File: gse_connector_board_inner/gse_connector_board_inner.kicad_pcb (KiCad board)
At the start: 2 copper layers, 52 x 27 mm, 27 parts, among them J1 arming_connector, J2 gse_com_connector, J3 chg_connector, J4 Conn_02x03_Top_Bottom, J5 Conn_02x02_Top_Bottom, U7 ISO1044BD, U9 MCP2562-E-SN

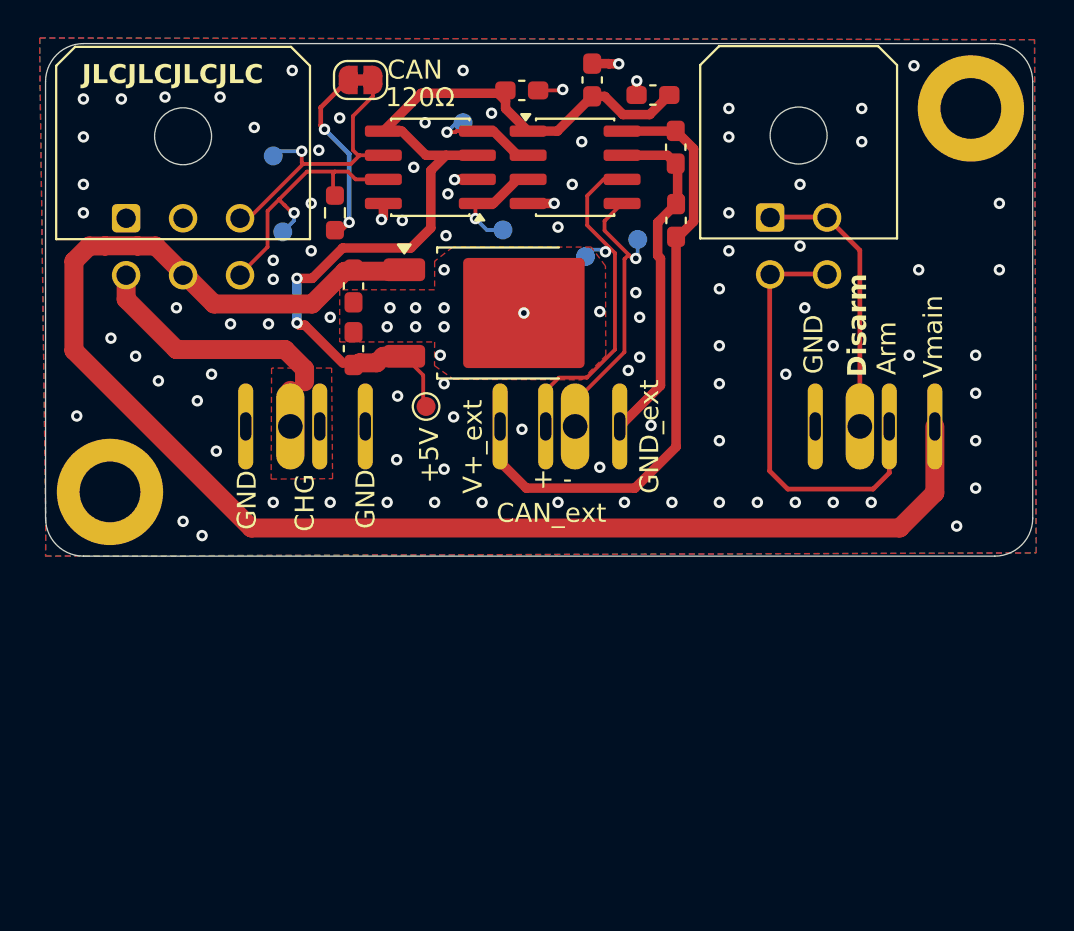
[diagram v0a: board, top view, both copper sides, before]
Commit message: first draft of rev3 with new pogo pins
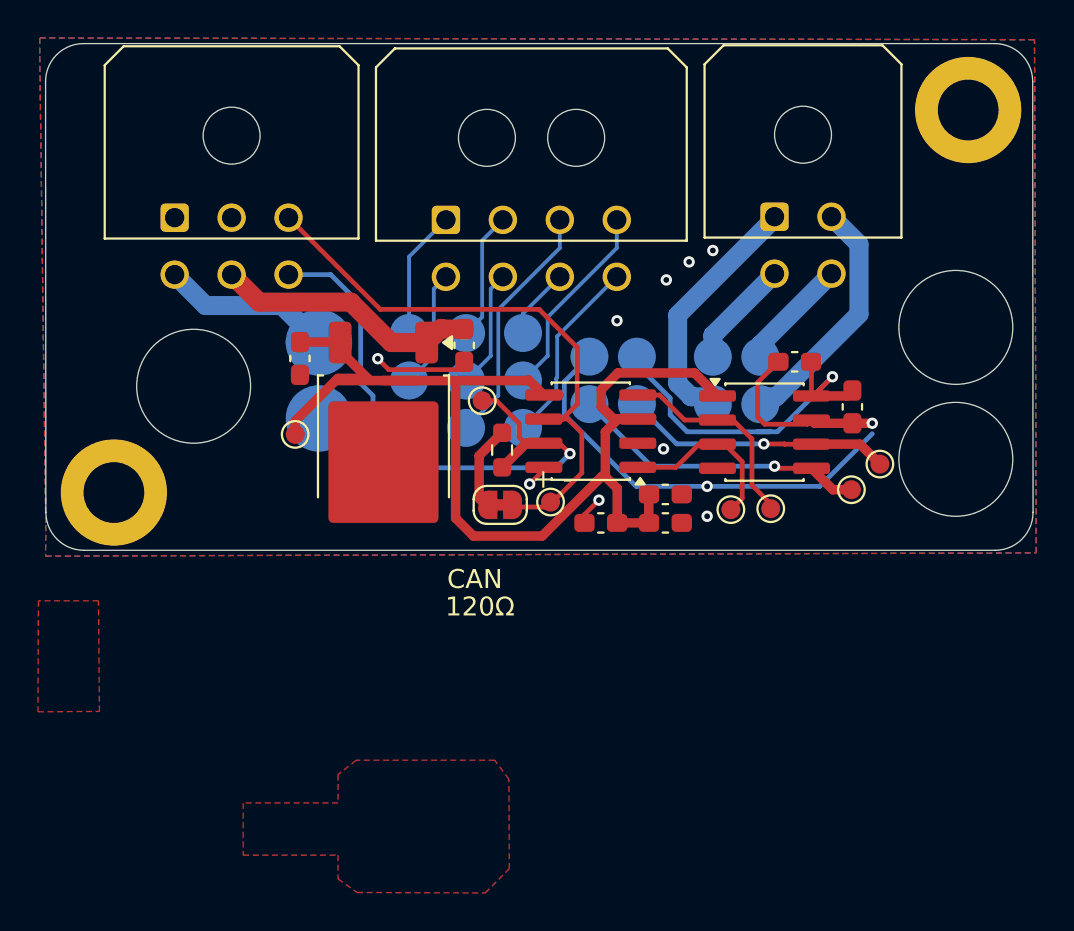
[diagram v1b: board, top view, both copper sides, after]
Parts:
- removed J1: arming_connector, custom_parts:4_pin_mag_con_new
- J2: value gse_com_connector -> Conn_01x19_Socket; footprint custom_parts:4_pin_mag_con_new -> custom_parts:tudsat_gse_connector_rev_1
- J3: value chg_connector -> ~; footprint custom_parts:4_pin_mag_con_new -> Connector_Molex:Molex_Micro-Fit_3.0_43045-0800_2x04_P3.00mm_Horizontal; moved to F.Cu
- TP1, TP2, TP3, TP4, TP5, TP6: moved to F.Cu
- moved H2 49.5 mm to (158.6, 56.5)
- moved H1 49.5 mm to (113.6, 76.7)
- moved TP5 26.0 mm to (148.2, 77.5), turned to 0 degrees
- moved JP4 23.6 mm to (133.9, 77.3)
- moved TP2 23.4 mm to (136.6, 77.2), turned to 0 degrees
- moved C29 23.3 mm to (139.2, 78.2), turned to 0 degrees
- moved C22 22.6 mm to (142.7, 76.8)
- moved C28 22.6 mm to (142.7, 78.2), turned to 180 degrees
- moved TP6 19.0 mm to (146.1, 77.5), turned to 0 degrees
- moved TP3 19.0 mm to (153.9, 75.2), turned to 0 degrees
- moved TP4 17.3 mm to (152.4, 76.5), turned to 0 degrees
- moved U7 17.2 mm to (147.9, 73.5)
- moved C24 16.5 mm to (152.5, 72.1)
- moved U9 16.3 mm to (138.7, 73.4)
- moved J3 16.1 mm to (131.1, 62.3), turned to 0 degrees
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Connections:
- J2 pad 1: +V_EXT -> arming_voltage
- J2 pad 2: CAN_ext+ -> arm
- J2 pad 3: CAN_ext- -> GND
- J2 pad 4: GND_EXT -> disarm
- J3 pad 1: GND -> TX+
- J3 pad 2: CHG -> RX+
- J3 pad 3: CHG -> NC1
- J3 pad 4: GND -> NC3
- J5 pad 1: disarm -> GND
- J5 pad 2: disarm -> arming_voltage
- J5 pad 3: arm -> disarm
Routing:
- net main_voltage: track 77.8 -> 14.1 mm
- net CAN_1+: track 14.5 -> 32.3 mm
- net CAN_1-: track 14.9 -> 31.9 mm, vias 1 -> 0
- net arm: track 22.9 -> 5.93 mm
- net GND_EXT: track 17.7 -> 32.4 mm, vias 0 -> 2
- net GND: track 6.94 -> 20.6 mm, vias 104 -> 9
- net +5V: track 47.3 -> 60.8 mm, vias 2 -> 0
- net NC1: track 0.00 -> 13.0 mm
- net arming_voltage: track 0.00 -> 12.8 mm
- net NC3: track 0.00 -> 10.5 mm
- net +V_EXT: track 30.4 -> 20.2 mm, vias 0 -> 1
- net NC4: track 0.00 -> 10.0 mm
- net disarm: track 14.8 -> 5.72 mm
- net RX+: track 0.00 -> 6.77 mm
- net TX+: track 0.00 -> 6.76 mm
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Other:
- board size 52 x 27 mm -> 52 x 26.7 mm
- board text added: "rev3"
- board text removed: "+5V"
- board text removed: "CAN_ext"
- board text removed: "GND_ext"
- board text removed: "GSE"
- board text removed: "JLCJLCJLCJLC"
- board text removed: "V+_ext"
- board text removed: "rev1"
